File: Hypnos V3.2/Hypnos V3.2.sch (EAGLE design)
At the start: 38 parts, among them Q1 NMOS, Q2 NMOS

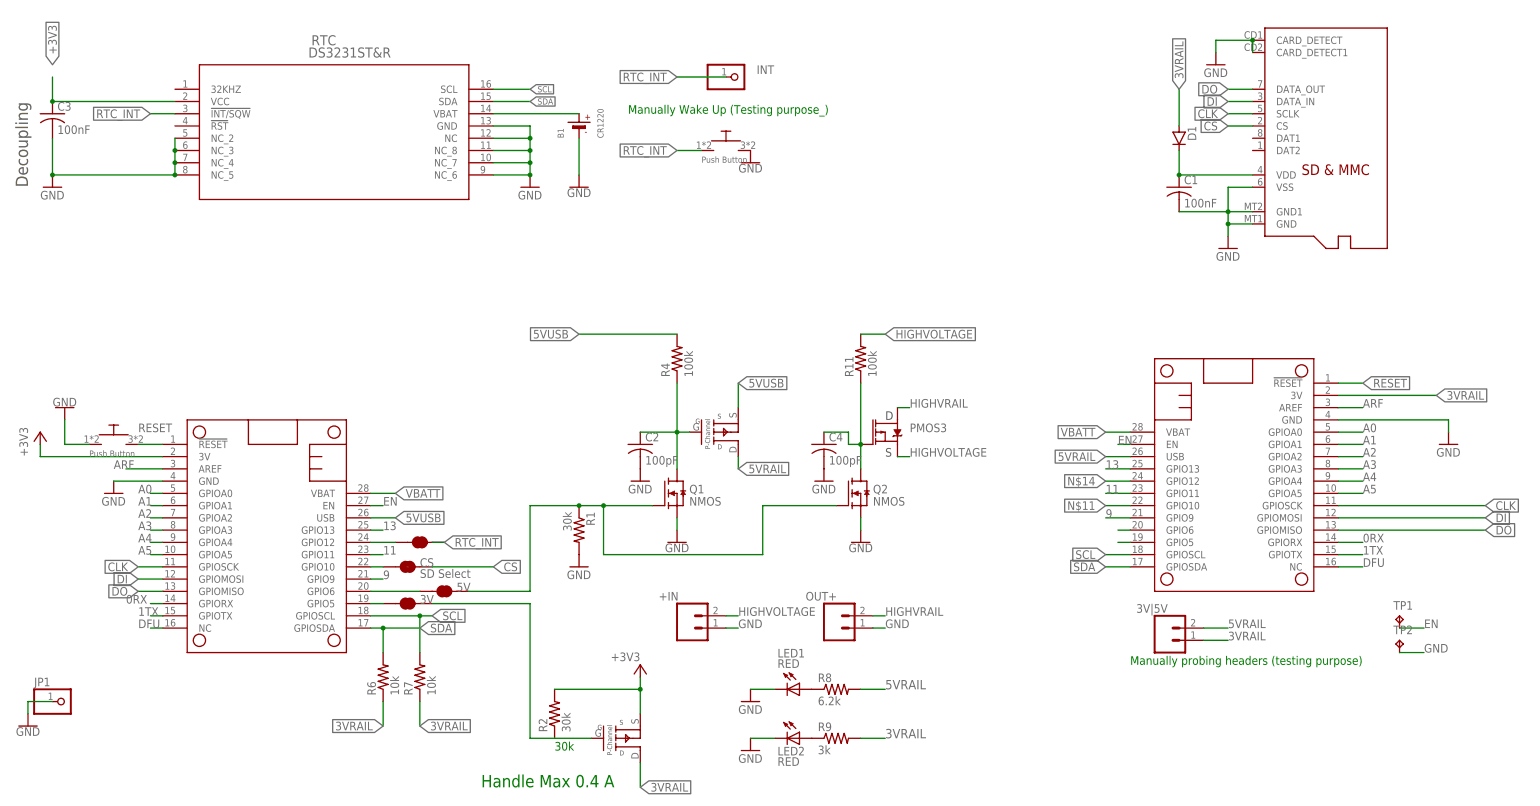
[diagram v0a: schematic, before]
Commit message: HardwareX documentation revision
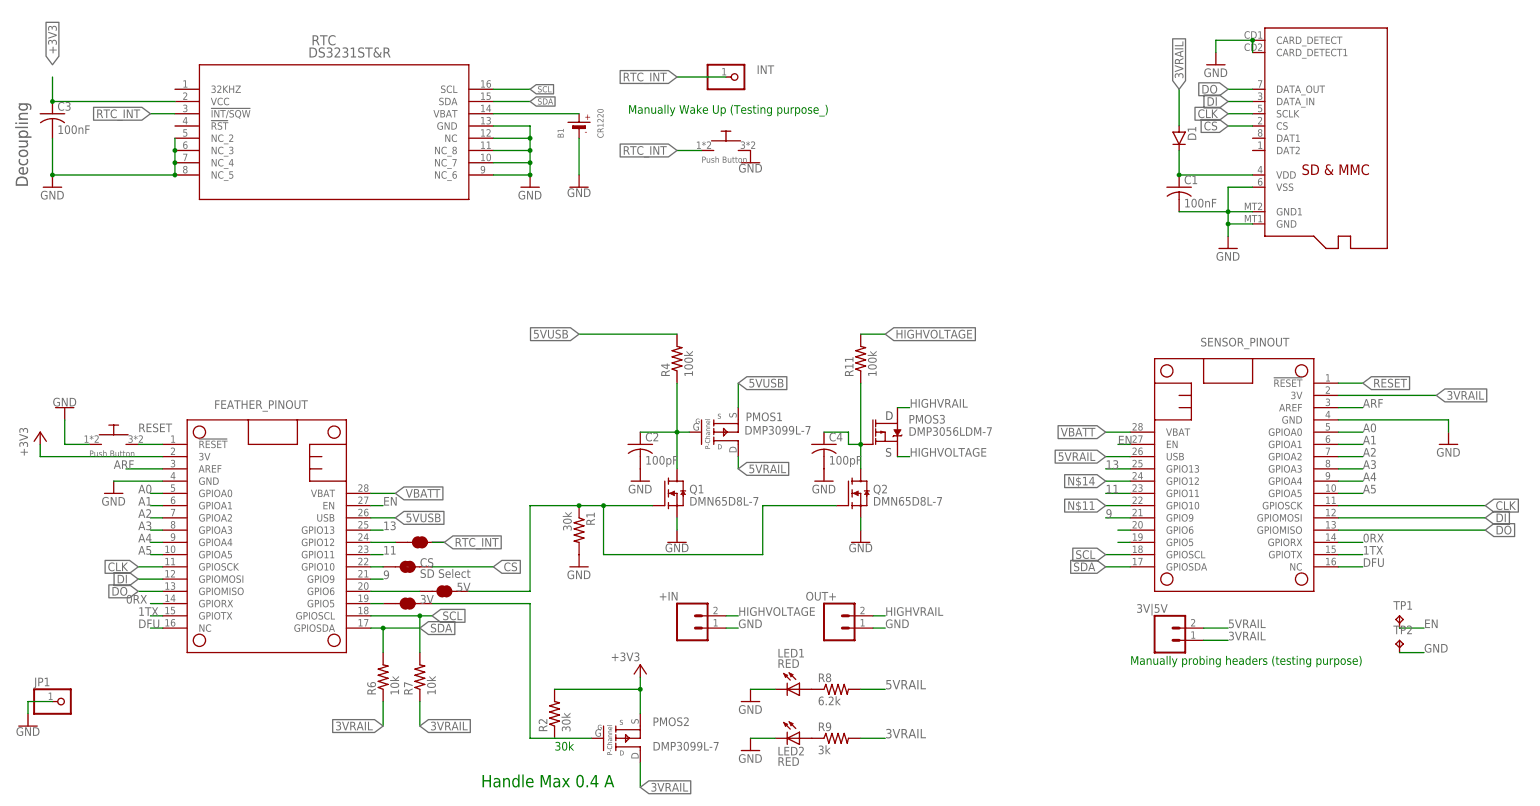
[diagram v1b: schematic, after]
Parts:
- FEATHERWING: value FEATHERWING -> SENSOR_PINOUT
- MS2: value FEATHERWING -> FEATHER_PINOUT
- PMOS1, PMOS2: value SSM3J3228R -> DMP3099L-7
- PMOS3: value P-MOSFET -> DMP3056LDM-7
- Q1, Q2: value NMOS -> DMN65D8L-7
- renumbered MS1 to FEATHERWING
